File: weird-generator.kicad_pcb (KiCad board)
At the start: 2 copper layers, 90 x 55 mm, 70 parts, among them J1 BATT, J2 OUT, Q1 2N3904, Q2 2N3904, SW1 Unusual, SW2 Unusual, SW3 Wacky, SW4 Wacky, SW5 Wacky Out, SW6 Wacky, SW7 ON/OFF, U1 40106, U3 LM741

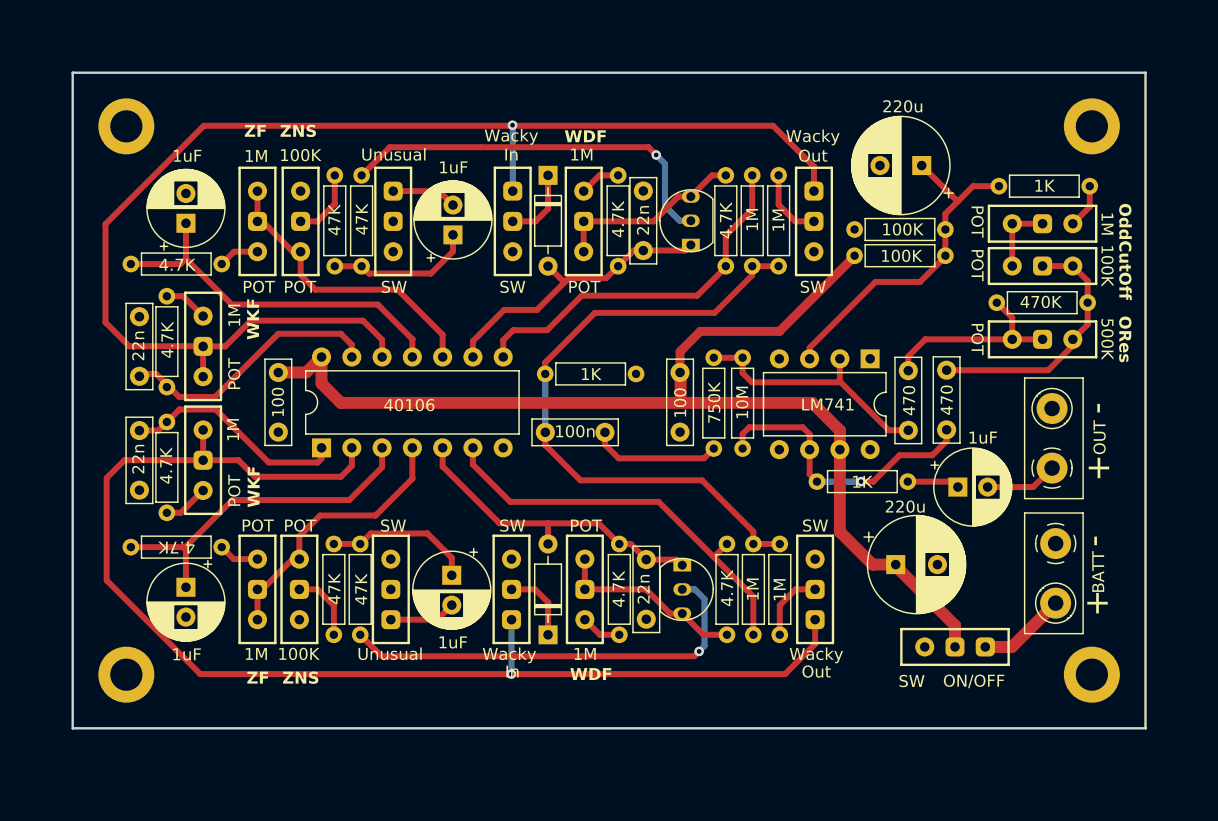
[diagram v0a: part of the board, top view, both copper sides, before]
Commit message: Redesigned to accommodate extra functionality
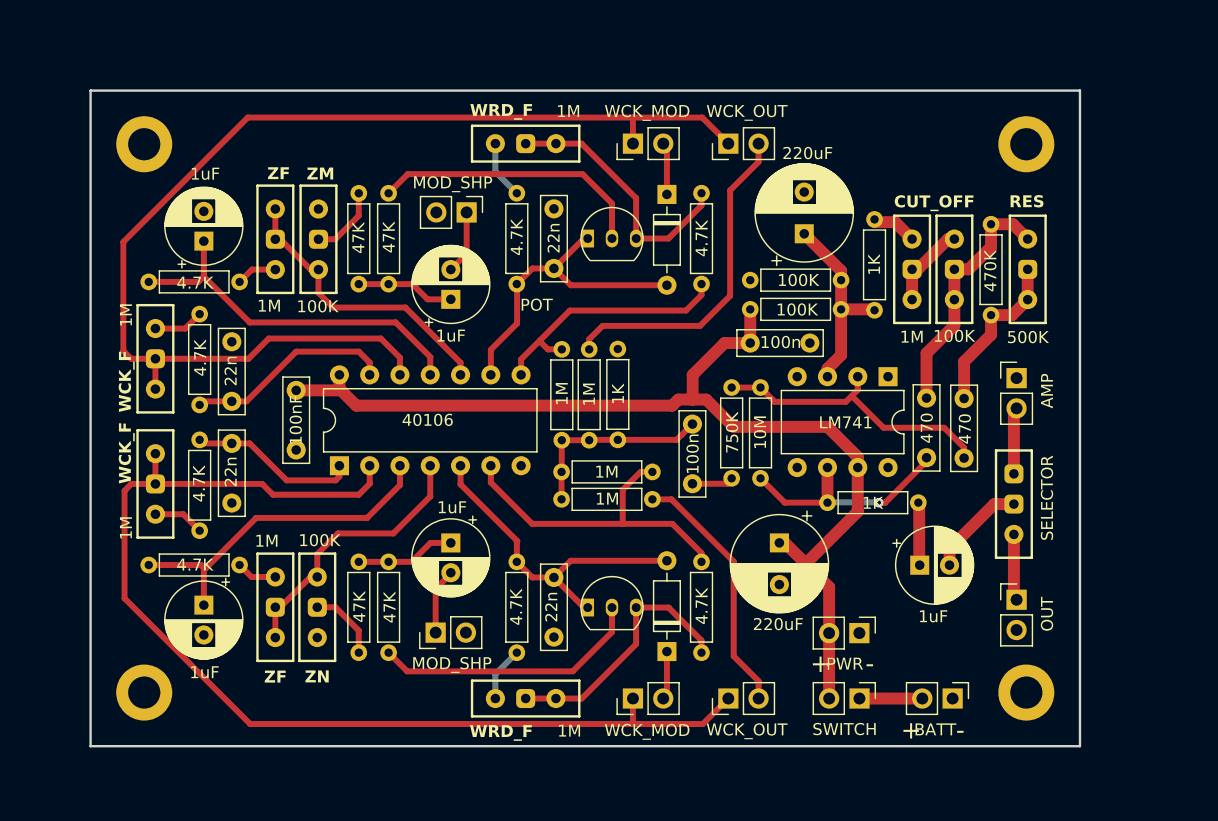
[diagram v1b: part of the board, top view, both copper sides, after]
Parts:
- added J3: AMP, Connector_PinHeader_2.54mm:PinHeader_1x02_P2.54mm_Vertical, F.Cu at (177.7, 74.1)
- added SW7: PWR, Connector_PinHeader_2.54mm:PinHeader_1x02_P2.54mm_Vertical, F.Cu at (164.5, 95.5)
- added SW8: SELECTOR, fx_synth_parts:switch_fx_connector, F.Cu at (177.5, 84.7)
- C10: value 100 -> 100nF
- C11, C13: value 220u -> 220uF
- C9: value 100 -> 100n
- J1, J2: footprint TerminalBlock_Phoenix:TerminalBlock_Phoenix_MKDS-1,5-2_1x02_P5.00mm_Horizontal -> Connector_PinHeader_2.54mm:PinHeader_1x02_P2.54mm_Vertical
- MOD_SHP: renamed from SW2; footprint fx_synth_parts:switch_fx_connector -> Connector_PinHeader_2.54mm:PinHeader_1x02_P2.54mm_Vertical
- MOD_SHP: renamed from SW1; footprint fx_synth_parts:switch_fx_connector -> Connector_PinHeader_2.54mm:PinHeader_1x02_P2.54mm_Vertical
- SW7: value ON/OFF -> SWITCH; footprint fx_synth_parts:switch_fx_connector -> Connector_PinHeader_2.54mm:PinHeader_1x02_P2.54mm_Vertical
- WCK_MOD: renamed from SW4; footprint fx_synth_parts:switch_fx_connector -> Connector_PinHeader_2.54mm:PinHeader_1x02_P2.54mm_Vertical
- WCK_MOD: renamed from SW3; footprint fx_synth_parts:switch_fx_connector -> Connector_PinHeader_2.54mm:PinHeader_1x02_P2.54mm_Vertical
- WCK_OUT: renamed from SW6; value Wacky -> Wacky Out; footprint fx_synth_parts:switch_fx_connector -> Connector_PinHeader_2.54mm:PinHeader_1x02_P2.54mm_Vertical
- WCK_OUT: renamed from SW5; footprint fx_synth_parts:switch_fx_connector -> Connector_PinHeader_2.54mm:PinHeader_1x02_P2.54mm_Vertical
- moved R16 21.6 mm to (139.5, 71.7)
- moved R15 21.6 mm to (141.8, 71.7)
- moved R22 18.3 mm to (165.8, 60.8), turned to -90 degrees
- moved R13 16.1 mm to (147.1, 82.0), turned to 180 degrees
- moved J1 15.6 mm to (172.3, 101.0)
- moved R14 15.6 mm to (147.1, 84.3), turned to 180 degrees
- moved WCK_MOD 13.7 mm to (145.5, 101.0)
- moved C12 12.4 mm to (150.5, 78.0), turned to -90 degrees
- moved WCK_MOD 12.0 mm to (145.5, 54.5), turned to 90 degrees
- moved WCK_OUT 11.7 mm to (153.5, 101.0)
- moved RV9 11.6 mm to (168.9, 65.0), turned to 0 degrees
- moved J2 11.4 mm to (177.7, 92.7), turned to 0 degrees
- moved C13 11.4 mm to (159.9, 62.0), turned to 90 degrees
- moved RV7 10.4 mm to (136.5, 101.0), turned to 90 degrees
- moved D2 10.1 mm to (148.3, 58.7)
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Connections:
- C16 pad 2: Net-(J2-Pin_1) -> /filter_out
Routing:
- net /filter in: track 54.5 -> 16.5 mm
- net Net-(SW6-B): track 6.01 -> 27.9 mm
- net Net-(SW5-B): track 5.99 -> 21.3 mm
- net Net-(SW4-A): track 109.5 -> 96.2 mm, vias 1 -> 0
- net Net-(Q1-B): track 36.1 -> 22.8 mm, vias 1 -> 0
- net Net-(SW3-A): track 105.1 -> 92.7 mm, vias 1 -> 0
- net Net-(U3-+): track 28.8 -> 16.6 mm
- net Net-(Q2-B): track 33.2 -> 23.4 mm, vias 1 -> 0
- net Net-(R12-Pad2): track 31.2 -> 21.8 mm
- net +BATT: track 96.9 -> 87.7 mm
- net /filter_out: track 0.00 -> 8.32 mm
- net Net-(C12-Pad2): track 11.0 -> 3.53 mm
- net Net-(Q2-C): track 16.1 -> 22.3 mm
- net Net-(R10-Pad2): track 34.3 -> 28.2 mm
- net Net-(Q1-C): track 16.0 -> 21.9 mm
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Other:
- board size 90 x 55 mm -> 83 x 55 mm
- board text added: "AUG 2025"
- board text added: "CUT_OFF"
- board text added: "RES"
- board text added: "SLICK"
- board text added: "VOLTS"
- board text added: "WCK_F"
- board text added: "WRD_F"
- board text added: "ZM"
- board text added: "ZN"
- board text removed: "Circuit Board by FX"
- board text removed: "In"
- board text removed: "ORes"
- board text removed: "OddCutOff"
- board text removed: "Out"
- board text removed: "SW"
- board text removed: "WDF"
- board text removed: "WKF"
- board text removed: "Wacky"
- board text removed: "Wacky Zany Weird Sound Generator"
- board text removed: "ZNS"

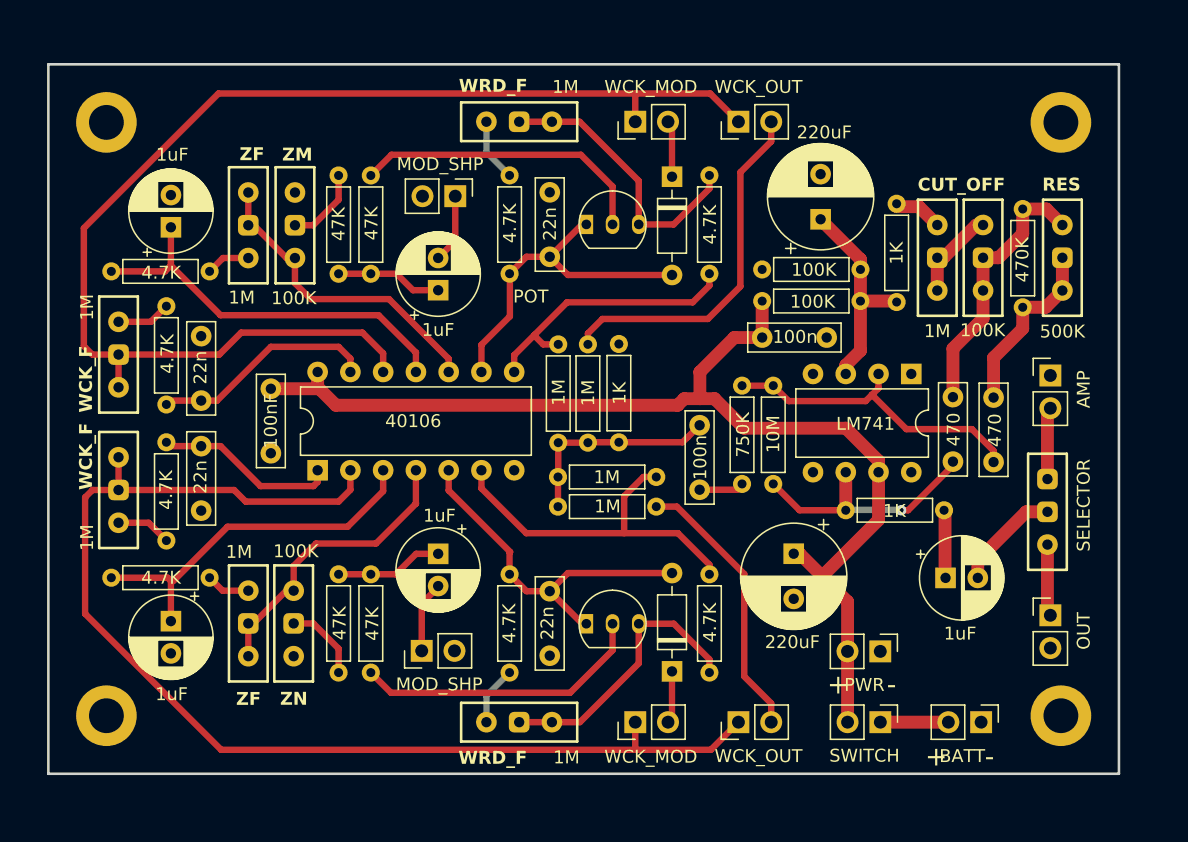
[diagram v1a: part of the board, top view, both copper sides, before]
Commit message: Added dual audio output and selector switch
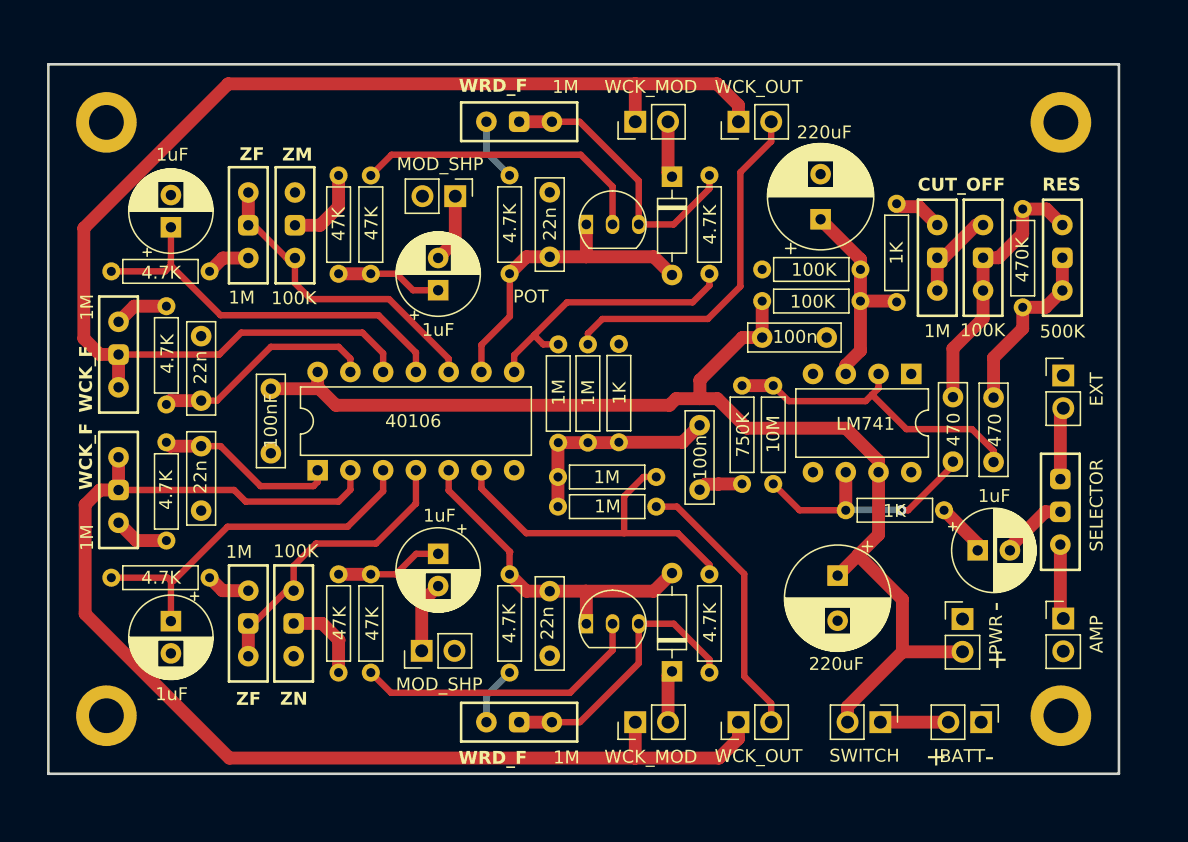
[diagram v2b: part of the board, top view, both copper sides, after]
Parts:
- J2: value OUT -> AMP
- J3: value AMP -> EXT
- moved SW7 6.85 mm to (170.9, 93.0), turned to 0 degrees
- moved C11 3.80 mm to (161.2, 89.6)
- moved C16 3.28 mm to (172.0, 87.7)
- moved J2 1.03 mm to (178.7, 93.0)
- moved J3 1.00 mm to (178.7, 74.1)
- moved SW8 1.00 mm to (178.5, 84.7)
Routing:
- net +BATT: track 87.7 -> 92.5 mm
- net /filter_out: track 8.32 -> 5.30 mm
- net Net-(SW4-A): track 96.2 -> 97.9 mm
- net Net-(SW3-A): track 92.7 -> 94.3 mm
- net Net-(D2-A): track 26.1 -> 24.8 mm
- net Net-(D1-A): track 27.7 -> 26.3 mm
- net Net-(C16-Pad1): track 5.34 -> 4.23 mm
